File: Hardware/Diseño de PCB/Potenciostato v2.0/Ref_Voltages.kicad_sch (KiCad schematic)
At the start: 17 parts, among them IC6 LM4040AIM3X-2.5_NOPB, IC7 LM4040A50IDBZR, IC8 OPA354AIDBVT

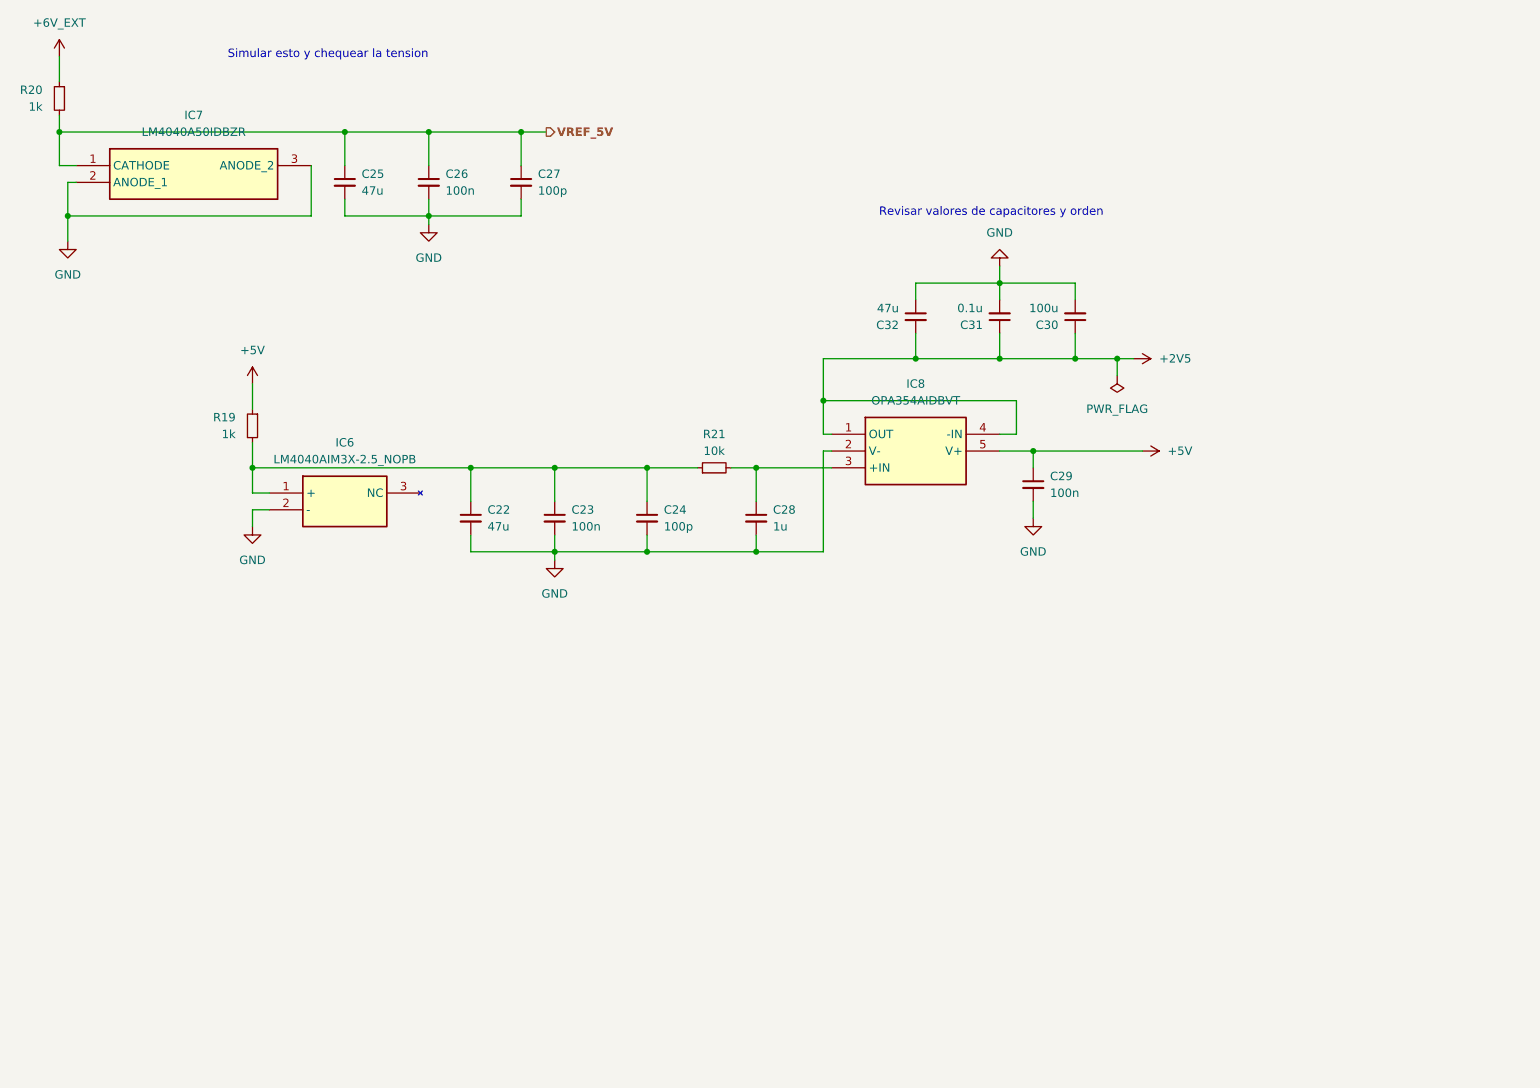
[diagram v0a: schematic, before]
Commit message: Big commit. Hardware was already ready. Board arrived. Hardware testing phase and software development is ongoing, some hardware issues were detected and noted down in the KiCad project for future versions and design corrections. First software libraries under development for ADC, GPIO, Muxes and DAC managment (ADS1255, MAX5217, MAX4737, MAX4617 and GPIO)
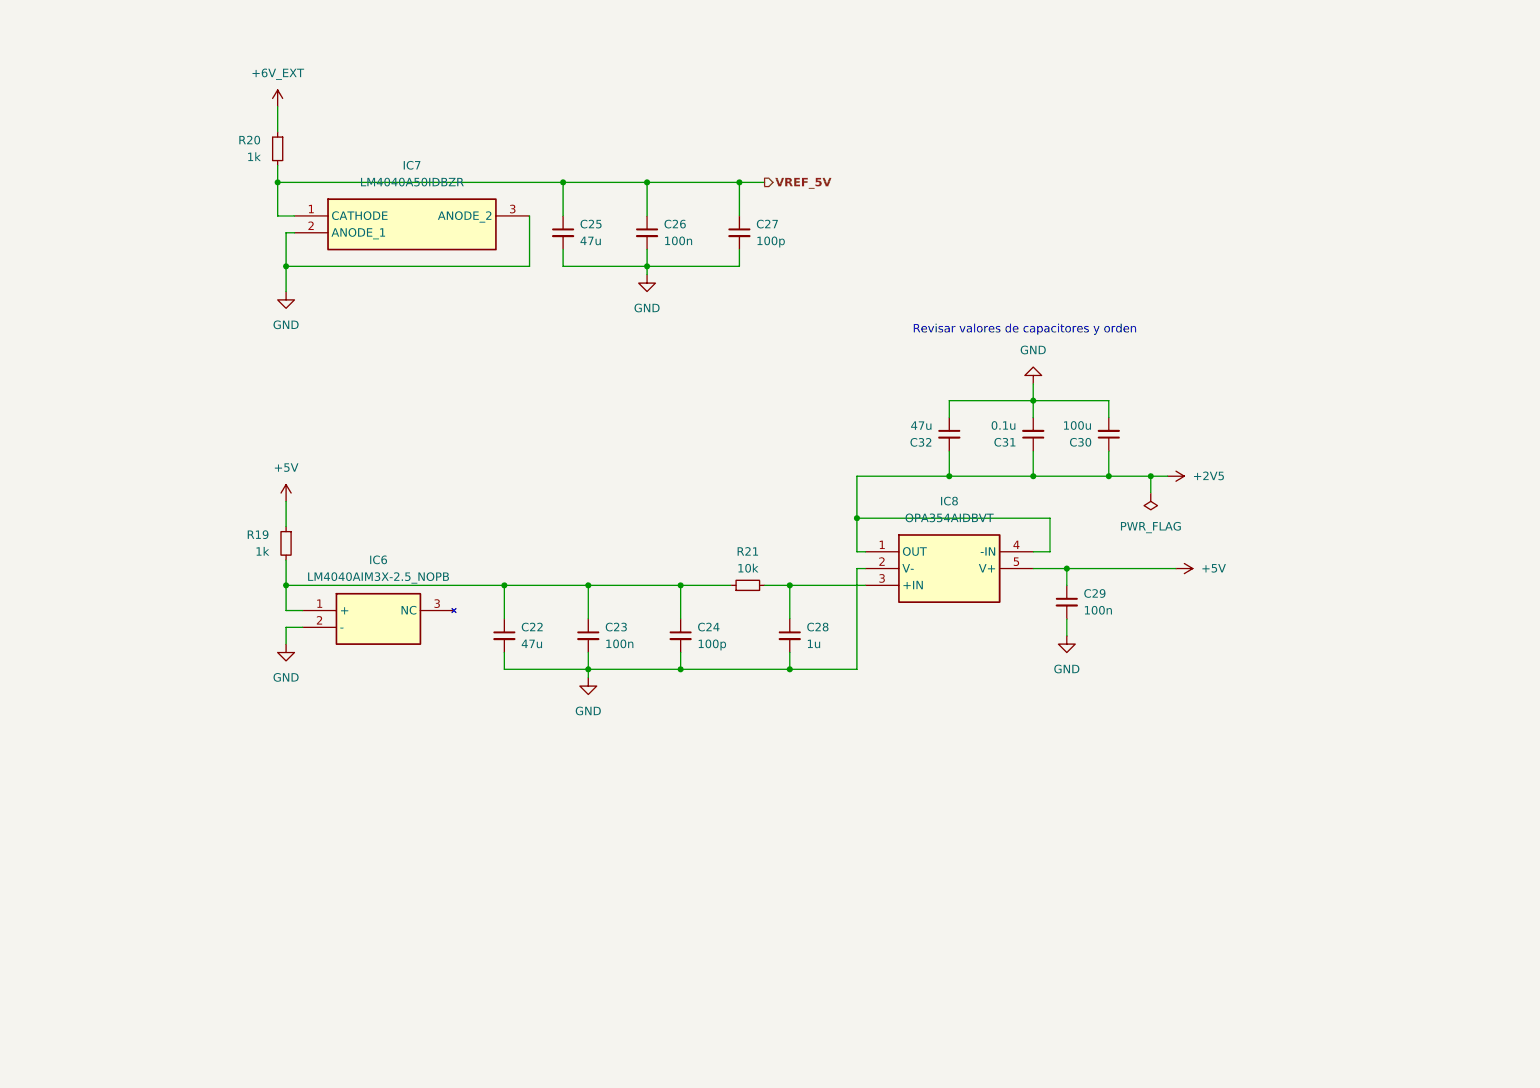
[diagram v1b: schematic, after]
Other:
- note removed: "Simular esto y chequear la tension"
- moved on the sheet: C22, C23, C24, C25, C26, C27, C28, C29, C30, C31, C32, IC6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

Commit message: Hardware modifications. More notes added to the KiCad project related to hardware issues found during testing. USB Power and ground inverted corrected in design and PCB. MAX4477 replaced by OPA2320 in design and PCB. More notes with recommendations and advised can now be found in the schematics.
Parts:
- C30: value 100u -> 10u
- C31: value 0.1u -> 1u
- C32: value 47u -> 0.1u
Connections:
- net +2V5: now also C32.1; no longer C32.2
- net GND: now also C32.2; no longer C32.1
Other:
- note added: "LM4040A50 NEEDS A SUPPLY HIGHER THAN 5V A ND MINIMUN CATHODE CURRENT OF AT LEAST 45 uA TO BE ABLE TO DELIVER A 5V REFERENCE"
- note added: "OPA354 CONFIGURED AS BUFFEROR VOLTAGE FOLLOWER TO PROVIDE A MORE STABILIZE 2.5V REFERENCE. THIS CIRCUIT IS RECOMMENDED IN THE ADS1255 DATASHEET."
- note removed: "Revisar valores de capacitores y orden"
- moved on the sheet: C30, C31
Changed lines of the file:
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@@
 		)
 	)
-	(text "Revisar valores de capacitores y orden"
-		(exclude_from_sim no)
-		(at 194.31 68.072 0)
-		(effects
-			(font
-				(size 1.27 1.27)
-				(color 255 25 16 1)
-			)
-		)
-	)
-	(hierarchical_label "VREF_5V"
-		(shape output)
-		(at 154.94 45.72 0)
-		(fields_autoplaced yes)
+	(text "OPA354 CONFIGURED AS BUFFEROR VOLTAGE FOLLOWER TO PROVIDE A \nMORE STABILIZE 2.5V REFERENCE. THIS CIRCUIT IS RECOMMENDED IN\nTHE ADS1255 DATASHEET.\n"
+		(exclude_from_sim no)
+		(at 223.266 134.366 0)
 		(effects
 			(font
@@
 				(bold yes)
 			)
+		)
+	)
+	(text "LM4040A50 NEEDS A SUPPLY HIGHER THAN 5V A\nND MINIMUN CATHODE CURRENT OF AT LEAST 45 uA \nTO BE ABLE TO DELIVER A 5V REFERENCE"
+		(exclude_from_sim no)
+		(at 121.92 27.94 0)
+		(effects
+			(font
+				(size 1.27 1.27)
+				(thickness 0.254)
+				(bold yes)
+			)
+		)
+	)
+	(hierarchical_label "VREF_5V"
+		(shape output)
+		(at 154.94 45.72 0)
+		(fields_autoplaced yes)
+		(effects
+			(font
+				(size 1.27 1.27)
+				(thickness 0.254)
+				(bold yes)
+			)
 			(justify left)
 		)
@@
 		(lib_id "Device:C_Small")
 		(at 182.88 83.82 0)
+		(mirror x)
 		(unit 1)
 		(exclude_from_sim no)
@@
 		(dnp no)
 		(property "Reference" "C32"
-			(at 180.34 85.0965 0)
+			(at 180.34 82.5435 0)
 			(effects
 				(font
@@
 			)
 		)
-		(property "Value" "47u"
-			(at 180.34 82.5565 0)
+		(property "Value" "0.1u"
+			(at 180.34 85.0835 0)
 			(effects
 				(font
@@
 	(symbol
 		(lib_id "Device:C_Small")
-		(at 195.58 83.82 180)
-		(unit 1)
-		(exclude_from_sim no)
-		(in_bom yes)
-		(on_board yes)
-		(dnp no)
-		(fields_autoplaced yes)
+		(at 195.58 83.82 0)
+		(mirror x)
+		(unit 1)
+		(exclude_from_sim no)
+		(in_bom yes)
+		(on_board yes)
+		(dnp no)
 		(property "Reference" "C31"
-			(at 193.04 85.0838 0)
-			(effects
-				(font
-					(size 1.27 1.27)
-				)
-				(justify left)
-			)
-		)
-		(property "Value" "0.1u"
-			(at 193.04 82.5438 0)
-			(effects
-				(font
-					(size 1.27 1.27)
-				)
-				(justify left)
+			(at 193.04 82.5435 0)
+			(effects
+				(font
+					(size 1.27 1.27)
+				)
+				(justify right)
+			)
+		)
+		(property "Value" "1u"
+			(at 193.04 85.0835 0)
+			(effects
+				(font
+					(size 1.27 1.27)
+				)
+				(justify right)
 			)
 		)
@@
 	(symbol
 		(lib_id "Device:C_Small")
-		(at 207.01 83.82 180)
-		(unit 1)
-		(exclude_from_sim no)
-		(in_bom yes)
-		(on_board yes)
-		(dnp no)
-		(fields_autoplaced yes)
+		(at 207.01 83.82 0)
+		(mirror x)
+		(unit 1)
+		(exclude_from_sim no)
+		(in_bom yes)
+		(on_board yes)
+		(dnp no)
 		(property "Reference" "C30"
-			(at 204.47 85.0838 0)
-			(effects
-				(font
-					(size 1.27 1.27)
-				)
-				(justify left)
-			)
-		)
-		(property "Value" "100u"
-			(at 204.47 82.5438 0)
-			(effects
-				(font
-					(size 1.27 1.27)
-				)
-				(justify left)
-			)
-		)
+			(at 204.47 82.5435 0)
+			(effects
+				(font
+					(size 1.27 1.27)
+				)
+				(justify right)
+			)
+		)
+		(property "Value" "10u"
+			(at 204.47 85.0835 0)
+			(effects
+				(font
+					(size 1.27 1.27)
+				)
+				(justify right)
+			)
+		)

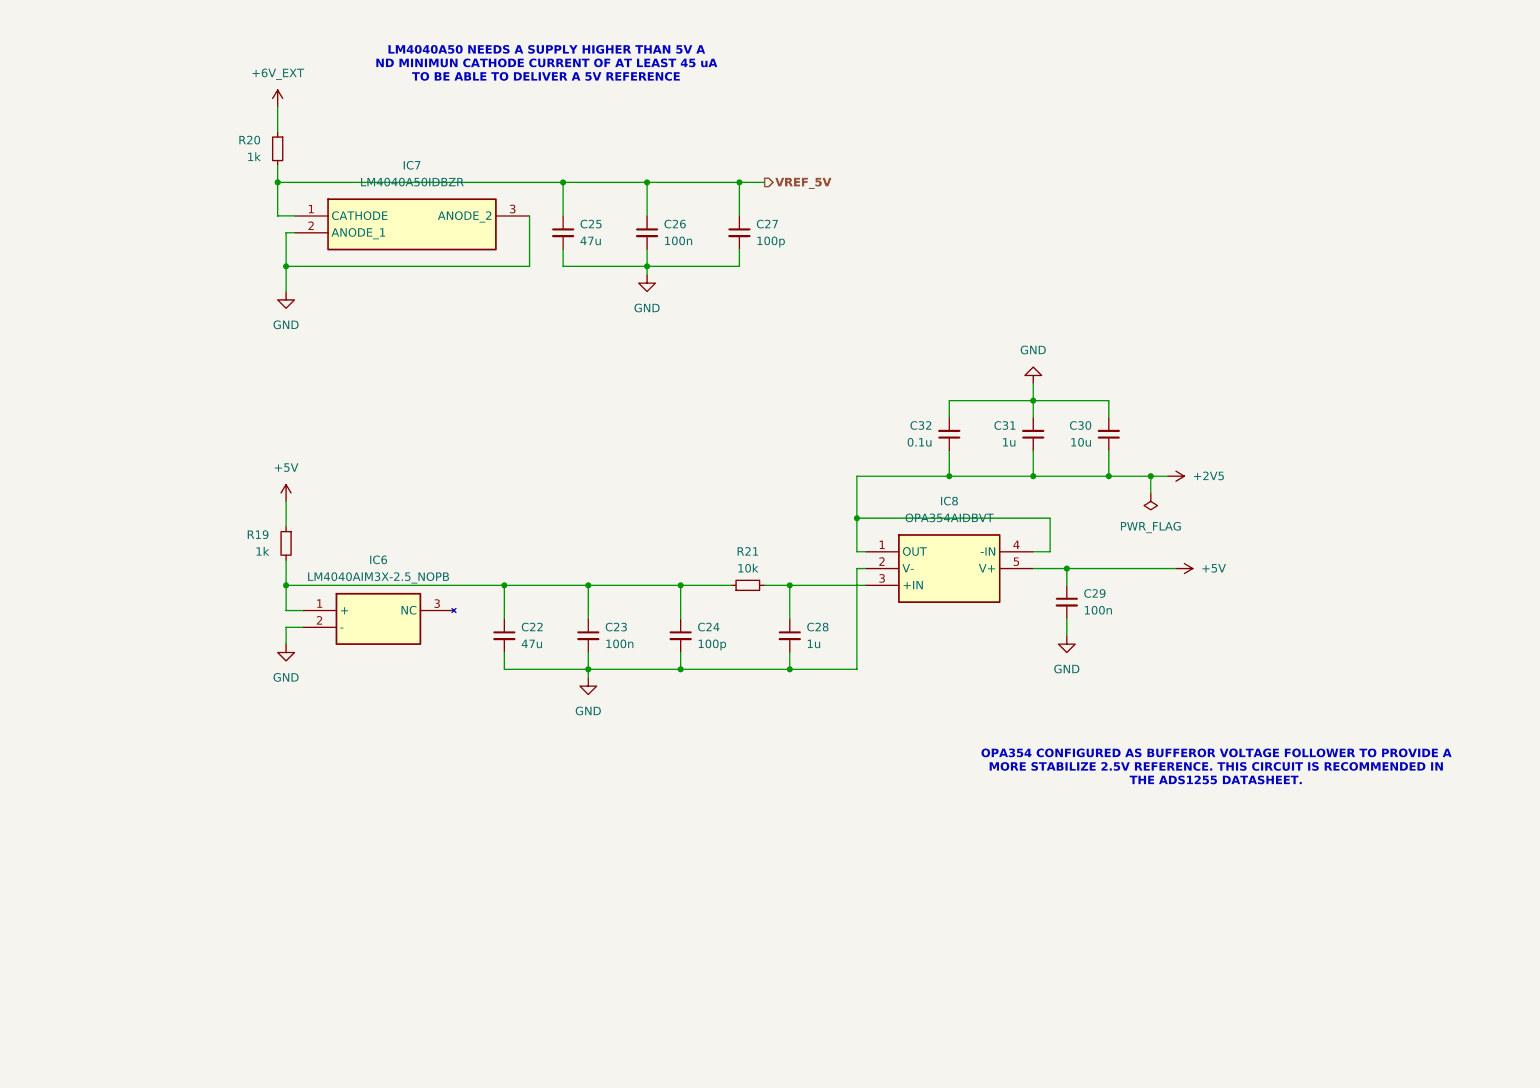
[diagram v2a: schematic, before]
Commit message: Further documentation and notes on the schematic. Software updates: In MAX4617, corrections in write function, more robust code verification to prevent overflows. In MUX, correction to MAX4617 gain codification and pinout updgraded for MAX4737. ADS1255, mux configured to AIN0-AINCOM in ADS_Initialized.
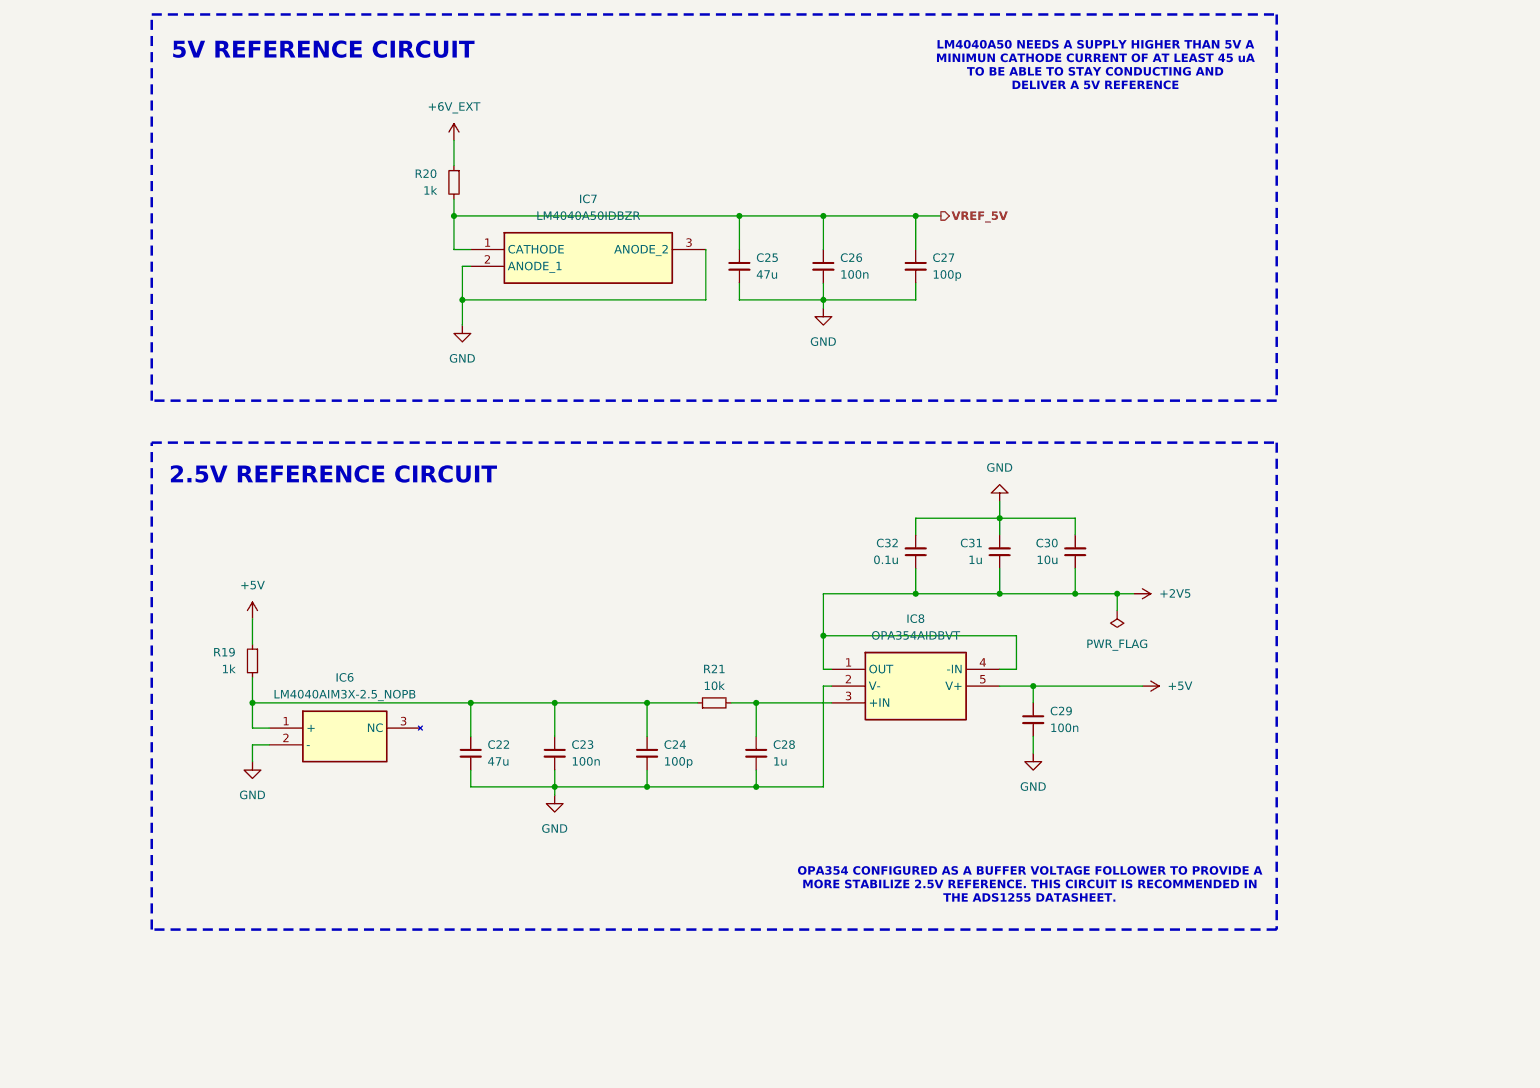
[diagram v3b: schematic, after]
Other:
- note added: "2.5V REFERENCE CIRCUIT"
- note added: "5V REFERENCE CIRCUIT"
- note added: "LM4040A50 NEEDS A SUPPLY HIGHER THAN 5V A MINIMUN CATHODE CURRENT OF AT LEAST 45 uA TO BE ABLE TO STAY CONDUCTING AND DELIVER A 5V REFERENCE"
- note added: "OPA354 CONFIGURED AS A BUFFER VOLTAGE FOLLOWER TO PROVIDE A MORE STABILIZE 2.5V REFERENCE. THIS CIRCUIT IS RECOMMENDED IN THE ADS1255 DATASHEET."
- note removed: "LM4040A50 NEEDS A SUPPLY HIGHER THAN 5V A ND MINIMUN CATHODE CURRENT OF AT LEAST 45 uA TO BE ABLE TO DELIVER A 5V REFERENCE"
- note removed: "OPA354 CONFIGURED AS BUFFEROR VOLTAGE FOLLOWER TO PROVIDE A MORE STABILIZE 2.5V REFERENCE. THIS CIRCUIT IS RECOMMENDED IN THE ADS1255 DATASHEET."
- moved on the sheet: C22, C23, C24, C25, C26, C27, C28, C29, C30, C31, C32, IC6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

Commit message: Hardware: Hardware Corrections in Potentiostat, small but important ones (WE electrode, Normal Open connection for electric disconnection in schematic and PCB. DAC I2C pull up resistors connected to 5V PCB layout corrected.). New project for ESP32 board: board design to hold ESP32 and LevelShifter for I2C3.3V to 5V. No more. No big changes in firmware and software, nothing to note, really small corrections in that were in the way.
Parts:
- added U11: ~, symbol Graphics_images:UNS_logo
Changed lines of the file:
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@@
+	)
+	(symbol
+		(lib_id "Graphics_images:UNS_logo")
+		(at 237.49 166.37 0)
+		(unit 1)
+		(exclude_from_sim no)
+		(in_bom no)
+		(on_board no)
+		(dnp yes)
+		(fields_autoplaced yes)
+		(property "Reference" "U11"
+			(at 236.728 161.798 0)
+			(effects
+				(font
+					(size 1.27 1.27)
+				)
+				(justify left)
+				(hide yes)
+			)
+		)
+		(property "Value" "~"
+			(at 217.17 157.48 0)
+			(effects
+				(font
+					(size 1.27 1.27)
+				)
+				(justify left)
+			)
+		)
+		(property "Footprint" ""
+			(at 228.6 162.56 0)
+			(effects
+				(font
+					(size 1.27 1.27)
+				)
+				(hide yes)
+			)
+		)
+		(property "Datasheet" ""
+			(at 228.6 162.56 0)
+			(effects
+				(font
+					(size 1.27 1.27)
+				)
+				(hide yes)
+			)
+		)
+		(property "Description" ""
+			(at 228.6 162.56 0)
+			(effects
+				(font
+					(size 1.27 1.27)
+				)
+				(hide yes)
+			)
+		)
+		(property "JLCLIB" ""
+			(at 237.49 166.37 0)
+			(effects
+				(font
+					(size 1.27 1.27)
+				)
+				(hide yes)
+			)
+		)
+		(instances
+			(project "Potenciostato v2.0"
+				(path "/3273751a-bb69-4014-b380-866ff743e010/89e5dcf3-4632-4140-92ed-deb05388ca59"
+					(reference "U11")
+					(unit 1)
+				)
+			)
+		)
 	)
 	(symbol
